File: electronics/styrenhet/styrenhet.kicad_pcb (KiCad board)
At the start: 2 copper layers, 16 parts, among them J1 Screw_Terminal_01x02, J2 Screw_Terminal_01x02, J3 Screw_Terminal_01x02, J4 Screw_Terminal_01x02, J5 Screw_Terminal_01x02, J6 Screw_Terminal_01x02, U1 motor_driver, U2 motor_driver, U3 motor_driver, U4 motor_driver

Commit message: Finish schematic:
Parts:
- added C10: 47uF, Capacitors_THT:CP_Radial_D10.0mm_P5.00mm, F.Cu at (132.6, 4.28)
- added C11: 47uF, Capacitors_THT:CP_Radial_D10.0mm_P5.00mm, F.Cu at (168.4, -5.87)
- added C12: 47uF, Capacitors_THT:CP_Radial_D10.0mm_P5.00mm, F.Cu at (180.1, -5.87)
- added C13: 0.1uF, Capacitors_SMD:C_0805_HandSoldering, F.Cu at (120.3, 11.6)
- added C14: 0.1uF, Capacitors_SMD:C_0805_HandSoldering, F.Cu at (125.8, 11.6)
- added C15: 0.1uF, Capacitors_SMD:C_0805_HandSoldering, F.Cu at (131.4, 11.6)
- added C16: 0.1uF, Capacitors_SMD:C_0805_HandSoldering, F.Cu at (136.9, 11.6)
- added C17: CP, Capacitors_THT:CP_Radial_D22.0mm_P10.00mm_SnapIn, F.Cu at (124.4, -13.5)
- added C18: CP, Capacitors_THT:CP_Radial_D22.0mm_P10.00mm_SnapIn, F.Cu at (160.5, -23.6)
- added C19: CP, Capacitors_THT:CP_Radial_D22.0mm_P10.00mm_SnapIn, F.Cu at (148.1, 0.13)
- added C20: CP, Capacitors_THT:CP_Radial_D22.0mm_P10.00mm_SnapIn, F.Cu at (184.3, -23.6)
- added C7: 47uF, Capacitors_THT:CP_Radial_D10.0mm_P5.00mm, F.Cu at (168.4, 5.88)
- added C8: 47uF, Capacitors_THT:CP_Radial_D10.0mm_P5.00mm, F.Cu at (144.6, -19.5)
- added C9: 47uF, Capacitors_THT:CP_Radial_D10.0mm_P5.00mm, F.Cu at (120.9, 4.28)
- added F1: Fuse, styrenhet-footprints:ETA_thl_fuseholder, F.Cu at (126.1, -27.9)
- added R1: 440R, Resistors_SMD:R_0603_HandSoldering, F.Cu at (147.1, 13.2)
- added R10: 660R, Resistors_SMD:R_0603_HandSoldering, F.Cu at (203.6, -29.3)
- added R11: 660R, Resistors_SMD:R_0603_HandSoldering, F.Cu at (167.5, 13.0)
- added R12: 660R, Resistors_SMD:R_0603_HandSoldering, F.Cu at (203.6, -26.8)
- added R13: 660R, Resistors_SMD:R_0603_HandSoldering, F.Cu at (203.6, -24.3)
- added R14: 660R, Resistors_SMD:R_0603_HandSoldering, F.Cu at (179.2, 3.72)
- added R15: 660R, Resistors_SMD:R_0603_HandSoldering, F.Cu at (203.6, -21.9)
- added R16: 660R, Resistors_SMD:R_0603_HandSoldering, F.Cu at (184.2, 1.24)
- added R2: 440R, Resistors_SMD:R_0603_HandSoldering, F.Cu at (142.2, 13.2)
- added R3: 440R, Resistors_SMD:R_0603_HandSoldering, F.Cu at (152.1, 13.2)
- added R4: 440R, Resistors_SMD:R_0603_HandSoldering, F.Cu at (203.6, -34.3)
- added R5: 440R, Resistors_SMD:R_0603_HandSoldering, F.Cu at (179.2, 1.24)
- added R6: 440R, Resistors_SMD:R_0603_HandSoldering, F.Cu at (203.6, -31.8)
- added R7: 440R, Resistors_SMD:R_0603_HandSoldering, F.Cu at (157.1, 13.2)
- added R8: 440R, Resistors_SMD:R_0603_HandSoldering, F.Cu at (191.0, -10.5)
- added R9: 660R, Resistors_SMD:R_0603_HandSoldering, F.Cu at (162.0, 13.2)
- C1, C2: footprint Capacitor_THT:CP_Radial_D22.0mm_P10.00mm_SnapIn -> Capacitors_THT:CP_Radial_D22.0mm_P10.00mm_SnapIn
- C3, C4: value 0.1uF -> CP; footprint Capacitor_SMD:C_1206_3216Metric_Pad1.42x1.75mm_HandSolder -> Capacitors_THT:CP_Radial_D22.0mm_P10.00mm_SnapIn
- C5, C6: value 0.1uF -> 47uF; footprint Capacitor_SMD:C_1206_3216Metric_Pad1.42x1.75mm_HandSolder -> Capacitors_THT:CP_Radial_D10.0mm_P5.00mm
- J1: value Screw_Terminal_01x02 -> 12V Fan; footprint styrenhet:TerminalBlock-XXL -> Pin_Headers:Pin_Header_Straight_1x04_Pitch2.54mm
- J2: value Screw_Terminal_01x02 -> Battery_In; footprint TerminalBlock:TerminalBlock_bornier-2_P5.08mm -> styrenhet-footprints:TerminalBlock-XXL
- J3: value Screw_Terminal_01x02 -> Battery to MCU; footprint TerminalBlock:TerminalBlock_bornier-2_P5.08mm -> TerminalBlocks_Phoenix:TerminalBlock_Phoenix_MKDS1.5-2pol
- J4: value Screw_Terminal_01x02 -> 12V Fan; footprint TerminalBlock:TerminalBlock_bornier-2_P5.08mm -> Pin_Headers:Pin_Header_Straight_1x04_Pitch2.54mm
- J5: value Screw_Terminal_01x02 -> IDE PATA Connector
- J6: value Screw_Terminal_01x02 -> Motor1_In
- U1: footprint styrenhet:motor-driver -> styrenhet-footprints:motor-driver
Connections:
- C1 pad 1: /BAT_+ -> /motor1+
- C1 pad 2: /BAT_- -> /motor1-
- C2 pad 1: /BAT_+ -> /motor2+
- C2 pad 2: /BAT_- -> /motor2-
- C3 pad 1: +5V -> /motor3+
- C3 pad 2: GND -> /motor3-
- C4 pad 1: +5V -> /motor4+
- C4 pad 2: GND -> /motor4-
- C5 pad 1: +5V -> /R_IS_1
- C6 pad 1: +5V -> /L_IS_1
- J1 pad 1: /BAT_+ -> GND
- J1 pad 2: /BAT_- -> Net-(F1-Pad1)
- J2 pad 2: /BAT_- -> GND
- J3 pad 1: /BAT_+ -> /B_MCU
- J3 pad 2: /BAT_- -> (no net)
- J4 pad 1: /BAT_+ -> GND
- J4 pad 2: /BAT_- -> Net-(F1-Pad1)
- J5 pad 1: /BAT_+ -> +5V
- J5 pad 2: /BAT_- -> +5V
- J6 pad 1: /BAT_- -> /motor1+
- J6 pad 2: /BAT_+ -> /motor1-
- U1 pad 1: (no net) -> /RPWM_1
- U1 pad 2: (no net) -> /LPWM_1
- U1 pad 3: (no net) -> /R_EN_1
- U1 pad 4: (no net) -> /L_EN_1
- U1 pad 5: +5V -> Net-(R9-Pad1)
- U1 pad 6: (no net) -> Net-(R10-Pad1)
- U2 pad 1: (no net) -> /RPWM_2
- U2 pad 2: (no net) -> /LPWM_2
- U2 pad 3: (no net) -> /R_EN_2
- U2 pad 4: (no net) -> /L_EN_2
- U2 pad 5: +5V -> Net-(R11-Pad1)
- U2 pad 6: (no net) -> Net-(R12-Pad1)
- U3 pad 1: (no net) -> /RPWM_3
- U3 pad 2: (no net) -> /LPWM_3
- U3 pad 3: (no net) -> /R_EN_3
- U3 pad 4: (no net) -> /L_EN_3
- U3 pad 5: +5V -> Net-(R13-Pad1)
- U3 pad 6: (no net) -> Net-(R14-Pad1)
- U4 pad 1: (no net) -> /RPWM_4
- U4 pad 2: (no net) -> /LPWM_4
- U4 pad 3: (no net) -> /R_EN_4
- U4 pad 4: (no net) -> /L_EN_4
- U4 pad 5: (no net) -> Net-(R15-Pad1)
- U4 pad 6: (no net) -> Net-(R16-Pad1)
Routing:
- net /BAT_+: track 252.2 -> 216.6 mm
- net /BAT_-: track 228.0 -> 202.9 mm

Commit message: Uppdatera footprints.
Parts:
- removed J5: IDE PATA Connector, TerminalBlock:TerminalBlock_bornier-2_P5.08mm
- added J7: Motor2_In, TerminalBlocks_Phoenix:TerminalBlock_Phoenix_MKDS1.5-2pol, F.Cu at (-88.0, -19.1)
- added J8: Motor3_In, TerminalBlocks_Phoenix:TerminalBlock_Phoenix_MKDS1.5-2pol, F.Cu at (-76.6, -19.1)
- added J9: Motor4_In, TerminalBlocks_Phoenix:TerminalBlock_Phoenix_MKDS1.5-2pol, F.Cu at (-63.6, -54.6)
- J6: footprint TerminalBlock:TerminalBlock_bornier-2_P5.08mm -> TerminalBlocks_Phoenix:TerminalBlock_Phoenix_MKDS1.5-2pol
- U2, U3, U4: footprint styrenhet:motor-driver -> styrenhet-footprints:motor-driver
- moved R8 339.0 mm to (-148.0, -7.97)
- moved J3 337.0 mm to (-63.6, -43.3)
- moved C1 335.1 mm to (-227.0, 70.2)
- moved C2 335.1 mm to (-115.2, 70.0)
- moved C3 335.1 mm to (-283.3, 98.2)
- moved C4 335.1 mm to (-166.4, 116.5)
- moved C5 335.1 mm to (-76.1, 113.4)
- moved C6 335.1 mm to (-222.0, 105.0)
- moved J1 335.1 mm to (-288.0, 71.0)
- moved J2 335.1 mm to (-62.5, 83.0)
- moved J4 335.1 mm to (-141.0, 70.0)
- moved C20 328.2 mm to (-143.6, -38.5)
- moved R4 327.6 mm to (-123.2, -11.8)
- moved C12 327.6 mm to (-147.1, -20.7)
- moved R10 322.5 mm to (-118.3, -9.28)
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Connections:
- J1 pad 3: Net-(J1-Pad3) -> (no net)
- J1 pad 4: Net-(J1-Pad4) -> (no net)
- J3 pad 2: (no net) -> /B_MCU
- J4 pad 3: Net-(J4-Pad3) -> (no net)
- J4 pad 4: Net-(J4-Pad4) -> (no net)
- R11 pad 1: Net-(R11-Pad1) -> (no net)
- R12 pad 1: Net-(R12-Pad1) -> (no net)
- R13 pad 1: Net-(R13-Pad1) -> (no net)
- R14 pad 1: Net-(R14-Pad1) -> (no net)
- R15 pad 1: Net-(R15-Pad1) -> (no net)
- R16 pad 1: Net-(R16-Pad1) -> (no net)
- U1 pad 1: /RPWM_1 -> (no net)
- U1 pad 2: /LPWM_1 -> (no net)
- U1 pad 3: /R_EN_1 -> (no net)
- U1 pad 4: /L_EN_1 -> (no net)
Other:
- board outline added: 160 x 100 mm

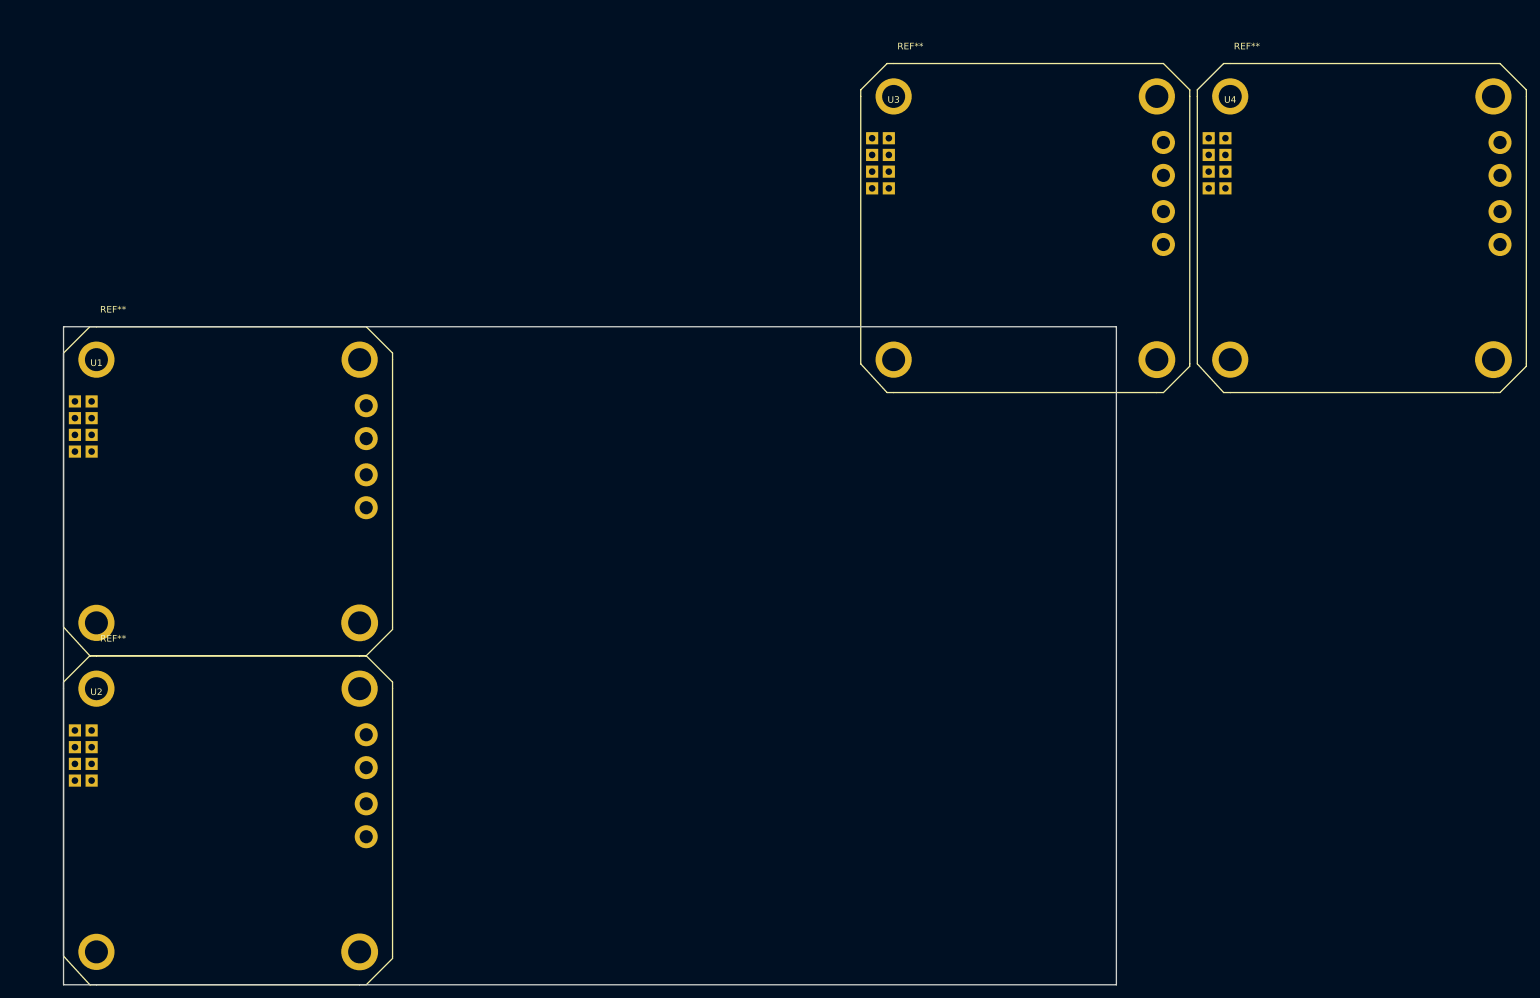
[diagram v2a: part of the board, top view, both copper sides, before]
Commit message: Placera h-bryggor.
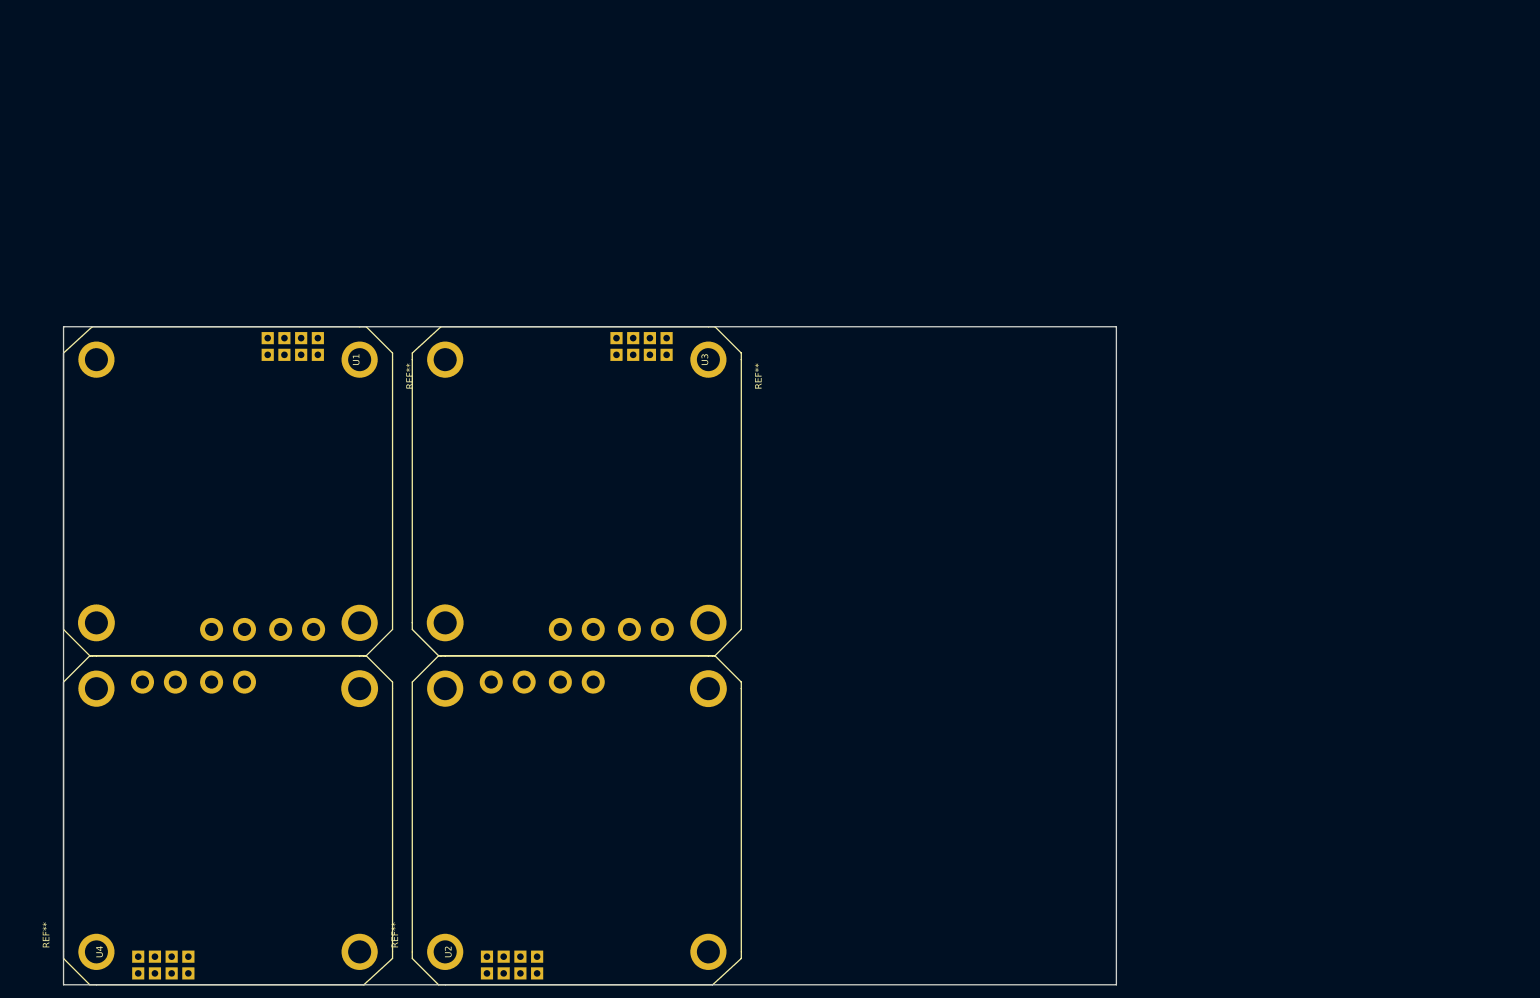
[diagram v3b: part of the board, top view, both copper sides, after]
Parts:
- moved U4 215.8 mm to (55.0, 145.0), turned to 90 degrees
- moved U2 66.4 mm to (108.0, 145.0), turned to 90 degrees
- moved U3 48.9 mm to (148.0, 55.0), turned to 270 degrees
- moved U1 40.0 mm to (95.0, 55.0), turned to 270 degrees

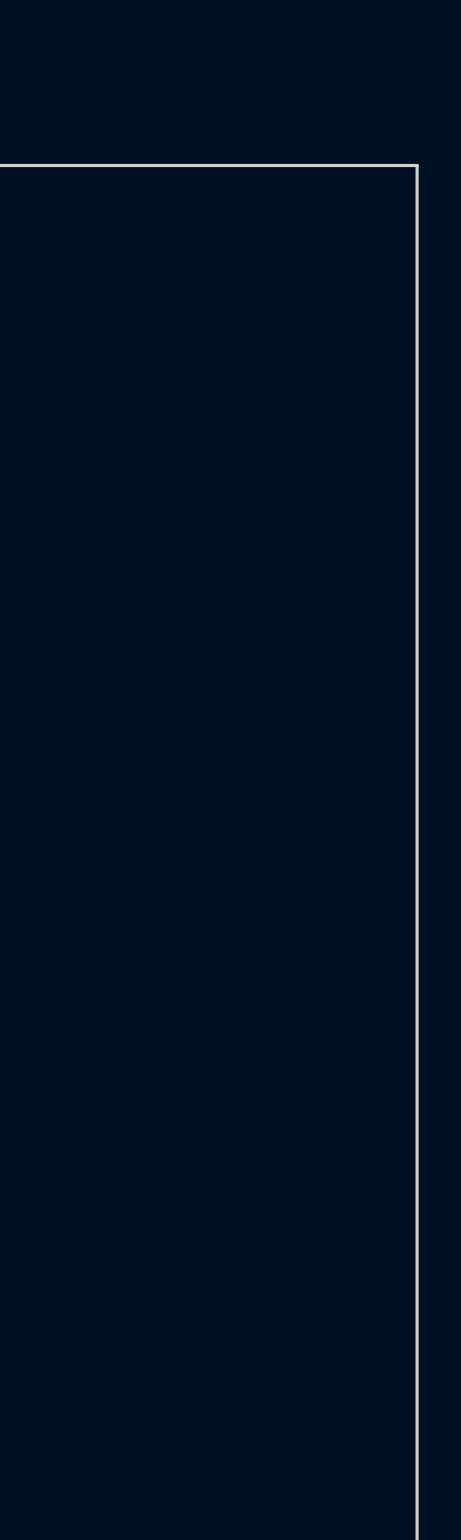
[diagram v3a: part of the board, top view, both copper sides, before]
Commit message: Add IDE PATA footprint.
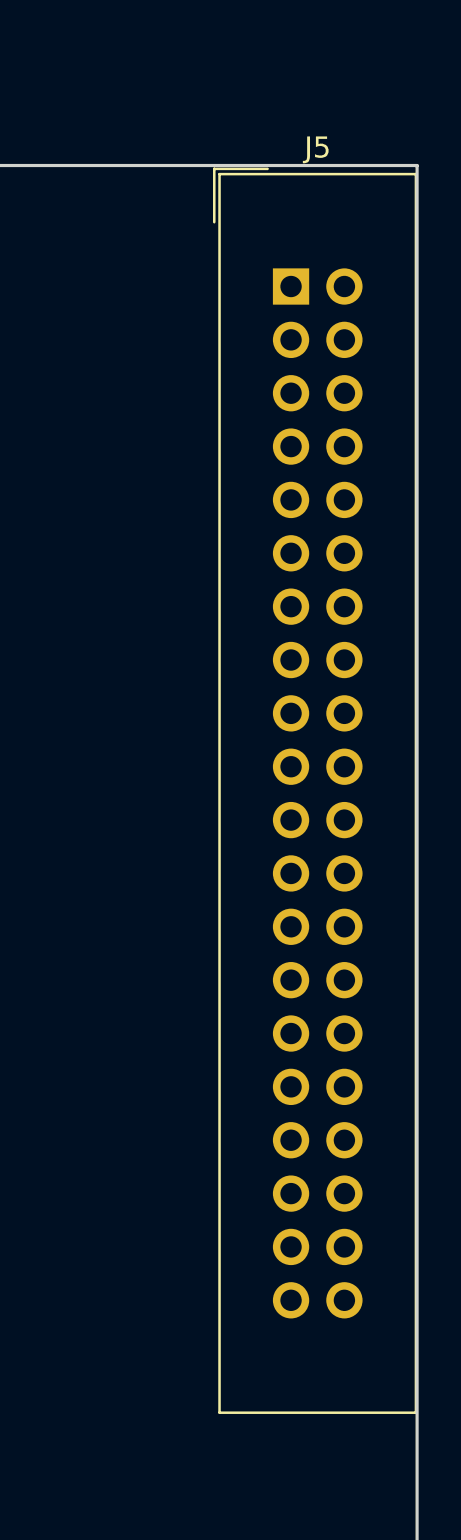
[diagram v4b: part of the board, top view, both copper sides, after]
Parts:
- added J5: IDE PATA Connector, styrenhet-footprints:IDC-Header_2x20_Pitch2.54mm_Straight, F.Cu at (204.0, 55.8)
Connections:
- R11 pad 1: (no net) -> Net-(R11-Pad1)
- R12 pad 1: (no net) -> Net-(R12-Pad1)
- R13 pad 1: (no net) -> Net-(R13-Pad1)
- R14 pad 1: (no net) -> Net-(R14-Pad1)
- R15 pad 1: (no net) -> Net-(R15-Pad1)
- R16 pad 1: (no net) -> Net-(R16-Pad1)
- U2 pad 1: /RPWM_2 -> (no net)
- U2 pad 2: /LPWM_2 -> (no net)
- U2 pad 3: /R_EN_2 -> (no net)
- U2 pad 4: /L_EN_2 -> (no net)
- U3 pad 1: /RPWM_3 -> (no net)
- U3 pad 2: /LPWM_3 -> (no net)
- U3 pad 3: /R_EN_3 -> (no net)
- U3 pad 4: /L_EN_3 -> (no net)
- U4 pad 1: /RPWM_4 -> (no net)
- U4 pad 2: /LPWM_4 -> (no net)
- U4 pad 3: /R_EN_4 -> (no net)
- U4 pad 4: /L_EN_4 -> (no net)

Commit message: Fortsätt routa komponenter.
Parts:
- moved C20 365.2 mm to (159.0, 166.0)
- moved R12 336.3 mm to (169.1, 189.0)
- moved C3 303.8 mm to (18.0, 59.5), turned to 270 degrees
- moved C18 293.8 mm to (100.5, 169.5)
- moved J3 279.0 mm to (197.5, 55.0), turned to 180 degrees
- moved C19 270.1 mm to (152.5, 24.5)
- moved C1 244.0 mm to (13.5, 111.5)
- moved C4 200.1 mm to (17.0, 36.5), turned to 270 degrees
- moved C17 198.3 mm to (100.0, 26.0)
- moved J6 183.2 mm to (55.0, 97.0), turned to 270 degrees
- moved J7 177.5 mm to (55.0, 86.0), turned to 270 degrees
- moved C5 170.6 mm to (-27.0, -50.0)
- moved J9 167.7 mm to (55.0, 64.0), turned to 270 degrees
- moved J8 161.7 mm to (55.0, 75.0), turned to 270 degrees
- moved F1 147.2 mm to (-157.0, 93.5)
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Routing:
- net /BAT_+: track 216.6 -> 0.00 mm
- net /BAT_-: track 202.9 -> 0.00 mm
- added copper zone on B.Cu, net /BAT_+
- added copper zone on F.Cu, net GND
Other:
- outline, holes or cut-outs redrawn
- net class Default: trace_width 0.25 -> 1; via_dia 0.8 -> 3; via_drill 0.4 -> 1

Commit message: Fortsätt routa
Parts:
- C13, C14, C15, C16, R1, R10, R11, R12, R13, R14, R15, R16, R2, R3, R4, R5, R6, R7, R8, R9: moved to B.Cu
- moved C6 372.5 mm to (150.5, 108.5), turned to 270 degrees
- moved C7 329.5 mm to (165.5, 114.0), turned to 270 degrees
- moved C13 322.0 mm to (158.0, 103.0), turned to 90 degrees
- moved R11 321.9 mm to (166.6, 109.1), turned to 270 degrees
- moved C15 318.9 mm to (158.0, 97.0), turned to 270 degrees
- moved R3 316.2 mm to (164.0, 109.1), turned to 270 degrees
- moved R2 307.0 mm to (152.0, 102.9), turned to 270 degrees
- moved R4 306.8 mm to (164.0, 96.1), turned to 90 degrees
- moved R1 306.2 mm to (152.0, 89.9), turned to 90 degrees
- moved R10 290.3 mm to (149.5, 102.9), turned to 270 degrees
- moved R9 290.2 mm to (149.5, 89.9), turned to 90 degrees
- moved C8 287.5 mm to (165.5, 92.0), turned to 90 degrees
- moved C11 282.6 mm to (112.5, 115.0), turned to 270 degrees
- moved C12 282.4 mm to (112.5, 90.5), turned to 90 degrees
- moved R8 279.1 mm to (111.0, 95.9), turned to 90 degrees
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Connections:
- J1 pad 3: (no net) -> Net-(J1-Pad3)
- J1 pad 4: (no net) -> Net-(J1-Pad4)
- J4 pad 3: (no net) -> Net-(J4-Pad3)
- J4 pad 4: (no net) -> Net-(J4-Pad4)
- U1 pad 1: (no net) -> /RPWM_1
- U1 pad 2: (no net) -> /LPWM_1
- U1 pad 3: (no net) -> /R_EN_1
- U1 pad 4: (no net) -> /L_EN_1
- U1 pad 7: (no net) -> +5V
- U2 pad 1: (no net) -> /RPWM_2
- U2 pad 2: (no net) -> /LPWM_2
- U2 pad 3: (no net) -> /R_EN_2
- U2 pad 4: (no net) -> /L_EN_2
- U2 pad 7: (no net) -> +5V
- U3 pad 1: (no net) -> /RPWM_3
- U3 pad 2: (no net) -> /LPWM_3
- U3 pad 3: (no net) -> /R_EN_3
- U3 pad 4: (no net) -> /L_EN_3
- U3 pad 7: (no net) -> +5V
- U4 pad 1: (no net) -> /RPWM_4
- U4 pad 2: (no net) -> /LPWM_4
- U4 pad 3: (no net) -> /R_EN_4
- U4 pad 4: (no net) -> /L_EN_4
- U4 pad 7: (no net) -> +5V
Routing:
- net /LPWM_1: track 0.00 -> 107.7 mm, vias 0 -> 2
- net /L_EN_1: track 0.00 -> 102.2 mm, vias 0 -> 2
- net /RPWM_1: track 0.00 -> 74.3 mm
- net /R_EN_1: track 0.00 -> 72.7 mm
- net /L_IS_1: track 0.00 -> 72.5 mm, vias 0 -> 2
- net /R_IS_1: track 0.00 -> 59.8 mm
- net /L_IS_4: track 0.00 -> 53.7 mm
- net /LPWM_3: track 0.00 -> 50.3 mm
- net /RPWM_3: track 0.00 -> 49.9 mm
- net /R_IS_4: track 0.00 -> 47.6 mm
- net /R_EN_3: track 0.00 -> 44.0 mm
- net /L_EN_3: track 0.00 -> 38.5 mm
- net /L_EN_4: track 0.00 -> 33.7 mm
- net /R_IS_3: track 0.00 -> 31.7 mm
- net /R_EN_4: track 0.00 -> 27.0 mm
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- added copper zone on F.Cu, net /BAT_+
- added copper zone on B.Cu, net GND
- removed copper zone on B.Cu, net /BAT_+
- removed copper zone on F.Cu, net GND

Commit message: Ännu mer
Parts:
- C18, C19, C20: moved to B.Cu
- moved C10 96.6 mm to (97.5, 109.5), turned to 270 degrees
- moved R14 73.3 mm to (96.5, 103.4), turned to 270 degrees
- moved R5 68.1 mm to (99.0, 90.0), turned to 90 degrees
- moved R6 68.1 mm to (99.0, 103.4), turned to 270 degrees
- moved C9 68.1 mm to (97.5, 84.0), turned to 90 degrees
- moved J9 68.0 mm to (55.0, 132.0)
- moved R13 64.5 mm to (96.5, 90.1), turned to 90 degrees
- moved C18 58.6 mm to (107.5, 139.5), turned to 180 degrees
- moved C19 54.5 mm to (110.0, 66.5)
- moved C20 38.1 mm to (160.0, 139.5), turned to 180 degrees
- moved J7 34.5 mm to (55.0, 120.5)
- moved J2 26.5 mm to (60.0, 101.0)
- moved J6 21.5 mm to (55.0, 75.5)
- moved J8 11.0 mm to (55.0, 64.0)
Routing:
- net +5V: track 17.8 -> 202.4 mm, vias 0 -> 2
- net /L_EN_3: track 38.5 -> 189.0 mm, vias 0 -> 2
- net /L_IS_4: track 53.7 -> 188.6 mm, vias 0 -> 2
- net /LPWM_3: track 50.3 -> 179.5 mm, vias 0 -> 2
- net /L_IS_3: track 24.8 -> 152.1 mm, vias 0 -> 2
- net /RPWM_3: track 49.9 -> 176.9 mm
- net /L_EN_4: track 33.7 -> 153.8 mm, vias 0 -> 2
- net /R_EN_3: track 44.0 -> 156.6 mm
- net /LPWM_4: track 22.0 -> 132.5 mm, vias 0 -> 2
- net /R_IS_4: track 47.6 -> 153.3 mm
- net /R_IS_3: track 31.7 -> 134.1 mm
- net /R_EN_4: track 27.0 -> 128.4 mm
- net /RPWM_4: track 16.6 -> 109.6 mm
- net GND: track 23.1 -> 79.1 mm
- net /L_IS_2: track 0.00 -> 55.9 mm, vias 0 -> 2
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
